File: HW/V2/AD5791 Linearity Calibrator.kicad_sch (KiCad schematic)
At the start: 47 parts, among them J11 PWR, J2 VREFP, J3 VREFN, J5 VREFP, SW1 RST, U11 L79L15, U12 7533, U13 ADuM1400xRW, U2 AD5791BRUZ, U3 ADR1399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

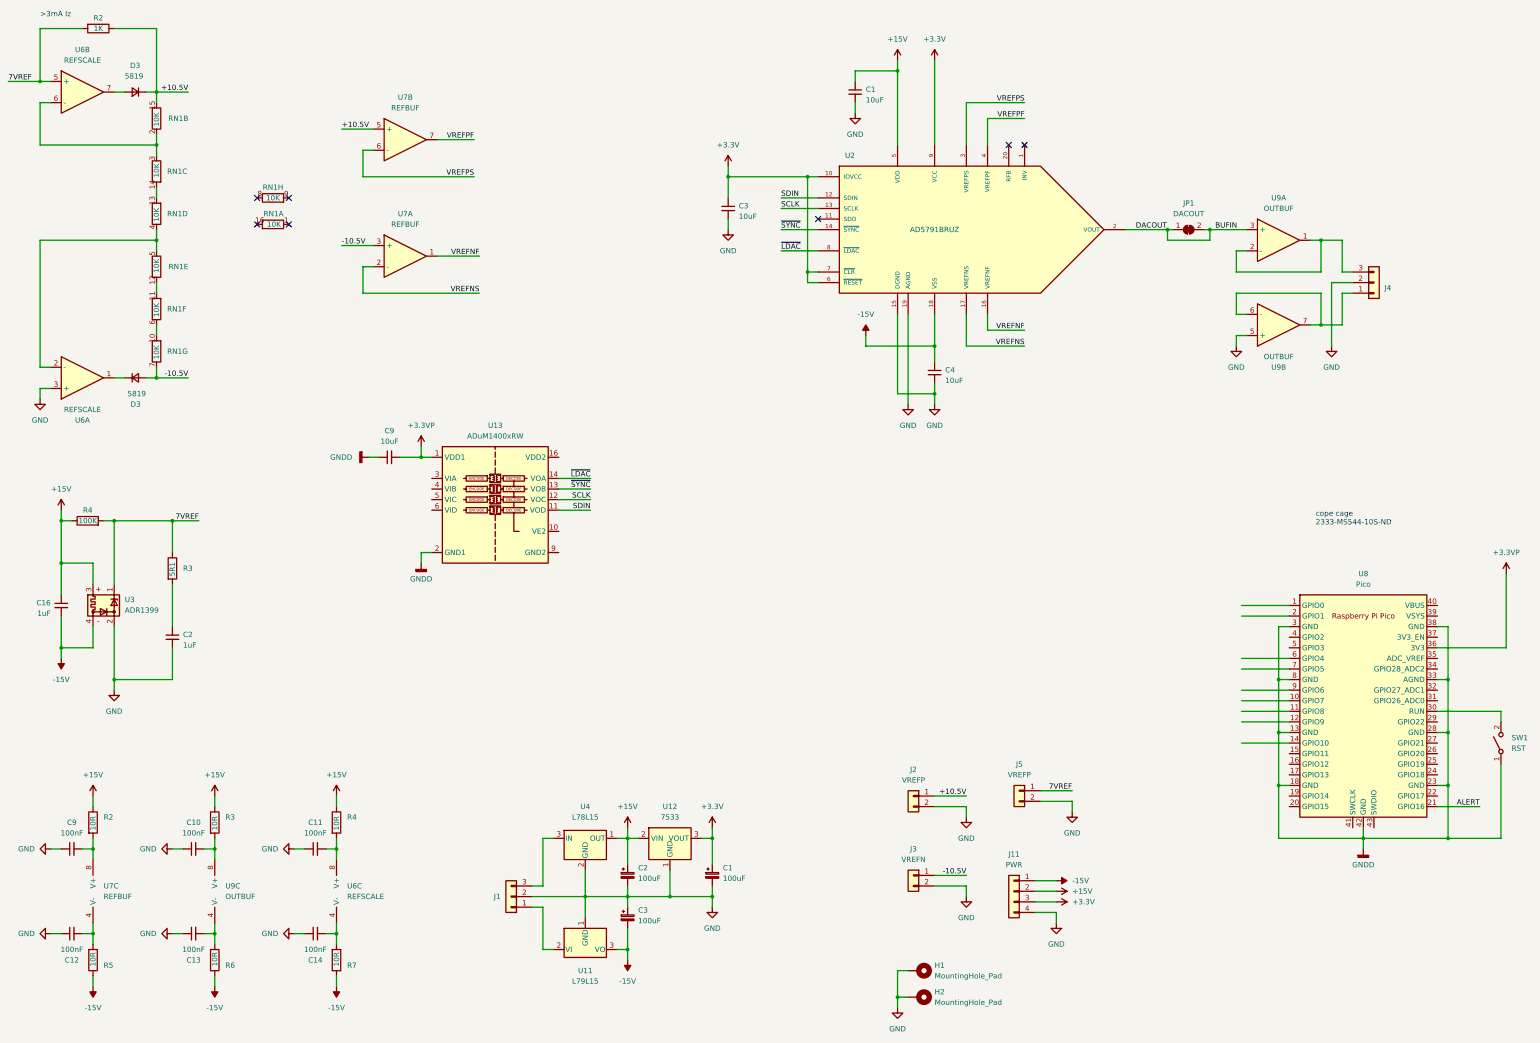
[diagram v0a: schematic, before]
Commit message: updated layout
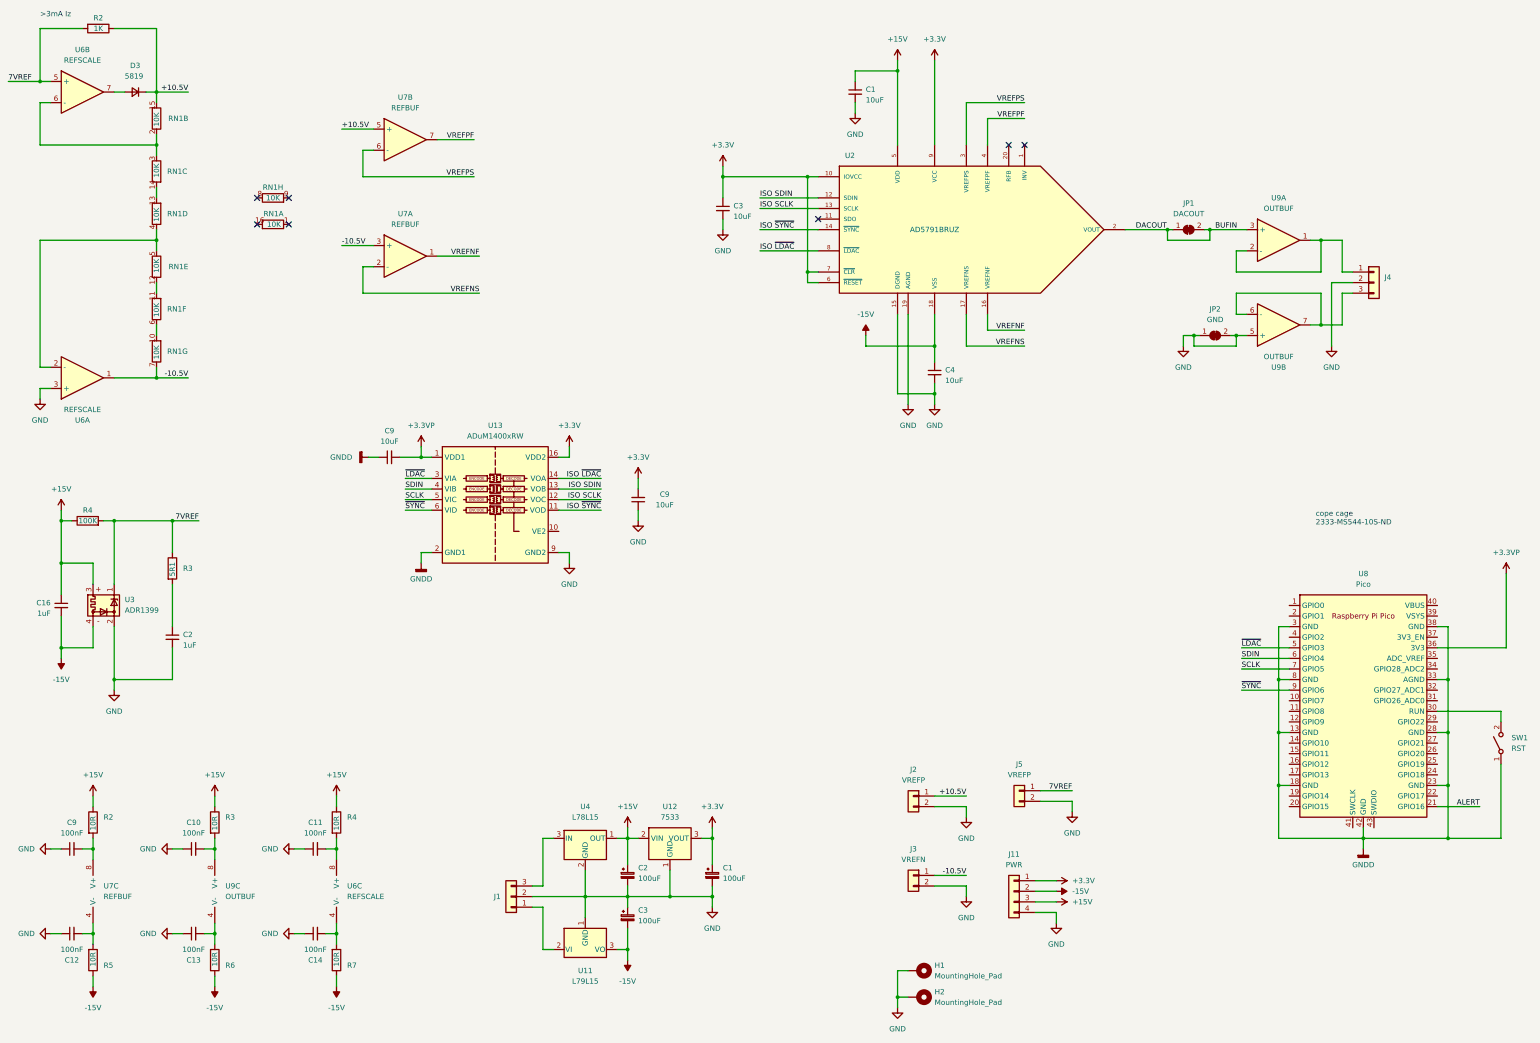
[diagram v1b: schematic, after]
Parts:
- removed D3: 5819, Resistor_SMD:R_0603_1608Metric_Pad0.98x0.95mm_HandSolder, symbol Device:D_Small
- added C9: 10uF, Resistor_SMD:R_0603_1608Metric, symbol Device:C_Small
- added JP2: GND, Connector_PinHeader_1.27mm:PinHeader_1x02_P1.27mm_Vertical, symbol Jumper:SolderJumper_2_Bridged
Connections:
- net +15V: now also J11.3 (Pin_3); no longer J11.2 (Pin_2)
- net +3.3V: now also J11.1 (Pin_1), U13.16 (VDD2), C9.2; no longer J11.3 (Pin_3)
- net -10.5V: now also U6.1
- net -15V: now also J11.2 (Pin_2); no longer J11.1 (Pin_1)
- net GND: now also U13.15 (GND2), U13.9 (GND2), C9.1, JP2.1 (A), JP2.2 (B)
- net SCLK: now also U13.5 (VIC), U8.7 (GPIO5); no longer U13.12 (VOC), U2.13 (SCLK)
- net SDIN: now also U13.4 (VIB), U8.6 (GPIO4); no longer U13.11 (VOD), U2.12 (SDIN)
- net ~{LDAC}: now also U13.3 (VIA), U8.5 (GPIO3); no longer U13.14 (VOA), U2.8 (~{LDAC})
- net ~{SYNC}: now also U13.6 (VID), U8.9 (GPIO6); no longer U13.13 (VOB), U2.14 (~{SYNC})
- net at U9.6 (-), U9.7: now also J4.3 (Pin_3); no longer J4.1 (Pin_1)
- net at U9.1, U9.2 (-): now also J4.1 (Pin_1); no longer J4.3 (Pin_3)
- new net ISO SCLK: U13.12 (VOC), U2.13 (SCLK)
- new net ISO SDIN: U13.13 (VOB), U2.12 (SDIN)
- new net ISO ~{LDAC}: U13.14 (VOA), U2.8 (~{LDAC})
- new net ISO ~{SYNC}: U13.11 (VOD), U2.14 (~{SYNC})
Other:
- moved on the sheet: C3

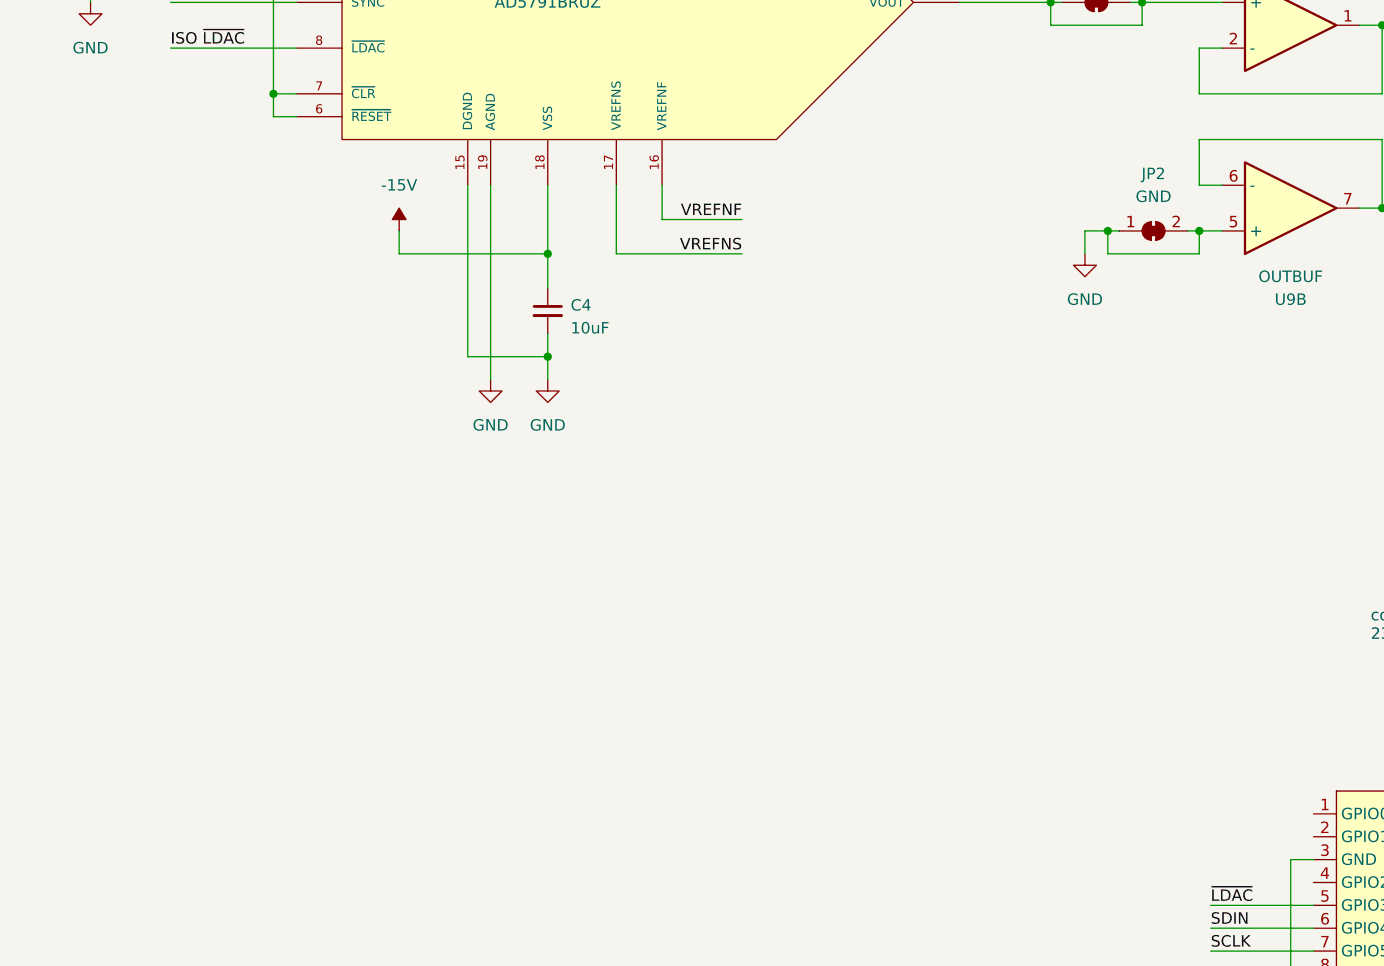
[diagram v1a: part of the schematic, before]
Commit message: updated layout
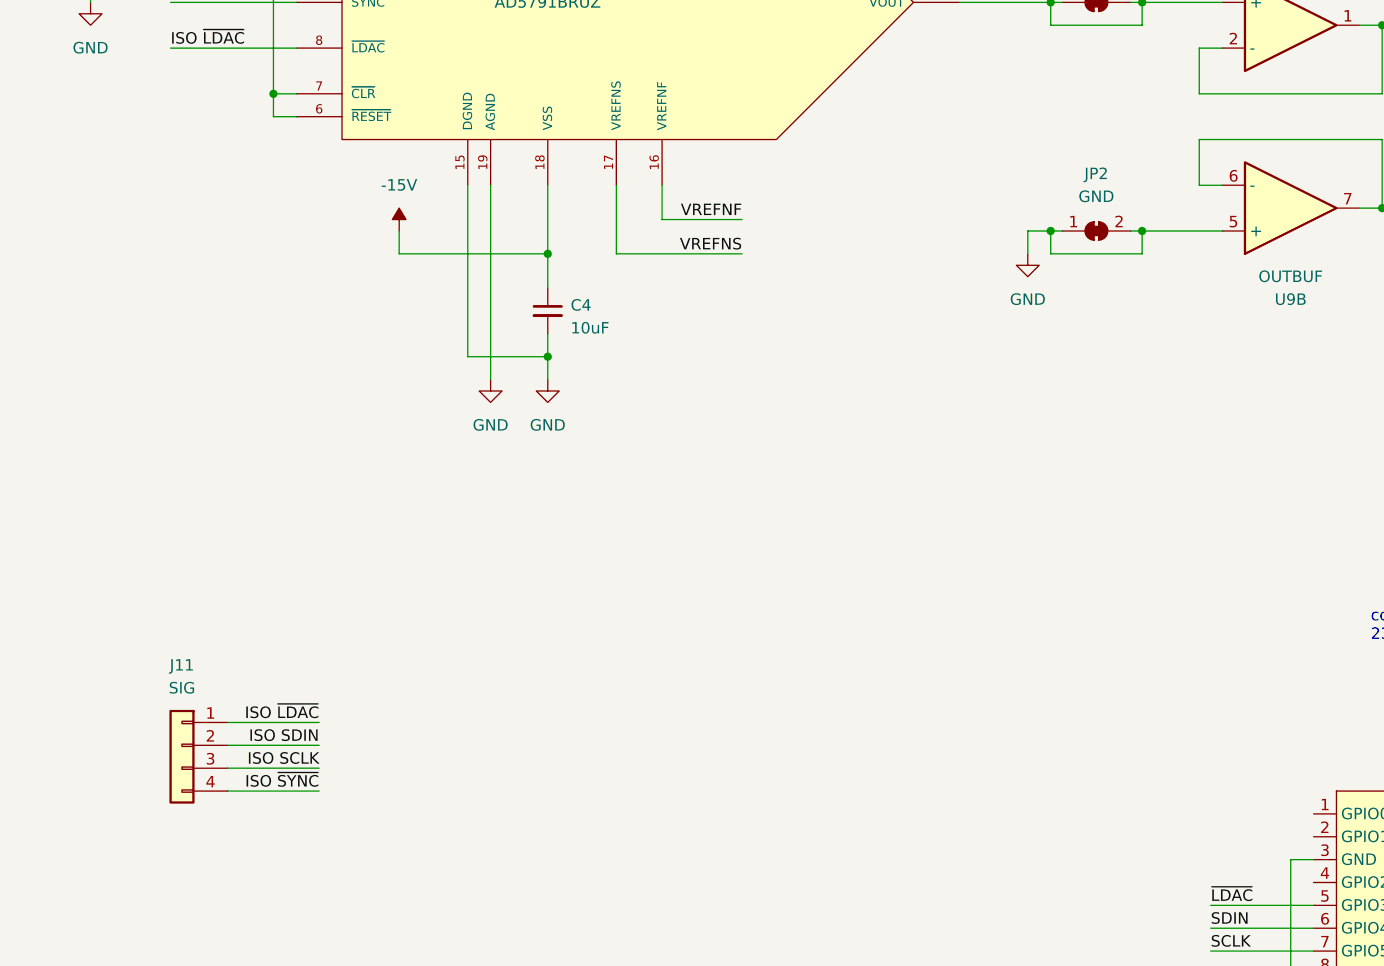
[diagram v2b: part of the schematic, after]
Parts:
- added J11: SIG, Connector_PinHeader_1.27mm:PinHeader_1x04_P1.27mm_Vertical, symbol Connector_Generic:Conn_01x04
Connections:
- net ISO SCLK: now also J11.3 (Pin_3)
- net ISO SDIN: now also J11.2 (Pin_2)
- net ISO ~{LDAC}: now also J11.1 (Pin_1)
- net ISO ~{SYNC}: now also J11.4 (Pin_4)
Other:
- moved on the sheet: JP2
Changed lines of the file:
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@@
 (kicad_sch (version 20230121) (generator eeschema)
   (paper "A3")
-  (junction (at 321.31 102.87) (diameter 0) (color 0 0 0 0)
-  )
   (junction (at 304.8 77.47) (diameter 0) (color 0 0 0 0)
   )
@@
   (junction (at 39.37 177.8) (diameter 0) (color 0 0 0 0)
   )
+  (junction (at 314.96 102.87) (diameter 0) (color 0 0 0 0)
+  )
   (junction (at 39.37 147.32) (diameter 0) (color 0 0 0 0)
   )
@@
   (junction (at 351.79 223.52) (diameter 0) (color 0 0 0 0)
   )
-  (junction (at 311.15 102.87) (diameter 0) (color 0 0 0 0)
+  (junction (at 304.8 102.87) (diameter 0) (color 0 0 0 0)
   )
   (junction (at 198.12 64.77) (diameter 0) (color 0 0 0 0)
@@
     (stroke (width 0) (type default))
   )
+  (wire (pts (xy 213.36 165.1) (xy 223.52 165.1))
+    (stroke (width 0) (type default))
+  )
   (wire (pts (xy 49.53 147.32) (xy 52.07 147.32))
     (stroke (width 0) (type default))
@@
     (stroke (width 0) (type default))
   )
+  (wire (pts (xy 213.36 157.48) (xy 223.52 157.48))
+    (stroke (width 0) (type default))
+  )
   (wire (pts (xy 158.75 144.78) (xy 168.91 144.78))
     (stroke (width 0) (type default))
@@
     (stroke (width 0) (type default))
   )
-  (wire (pts (xy 308.61 102.87) (xy 311.15 102.87))
+  (wire (pts (xy 302.26 102.87) (xy 304.8 102.87))
     (stroke (width 0) (type default))
   )
@@
     (stroke (width 0) (type default))
   )
-  (wire (pts (xy 320.04 102.87) (xy 321.31 102.87))
+  (wire (pts (xy 313.69 102.87) (xy 314.96 102.87))
     (stroke (width 0) (type default))
   )
@@
     (stroke (width 0) (type default))
   )
-  (wire (pts (xy 321.31 105.41) (xy 311.15 105.41))
+  (wire (pts (xy 314.96 105.41) (xy 304.8 105.41))
     (stroke (width 0) (type default))
   )
@@
     (stroke (width 0) (type default))
   )
-  (wire (pts (xy 321.31 102.87) (xy 323.85 102.87))
-    (stroke (width 0) (type default))
-  )
   (wire (pts (xy 341.63 80.01) (xy 346.71 80.01))
     (stroke (width 0) (type default))
@@
     (stroke (width 0) (type default))
   )
-  (wire (pts (xy 321.31 102.87) (xy 321.31 105.41))
+  (wire (pts (xy 314.96 102.87) (xy 314.96 105.41))
     (stroke (width 0) (type default))
   )
@@
     (stroke (width 0) (type default))
   )
+  (wire (pts (xy 213.36 162.56) (xy 223.52 162.56))
+    (stroke (width 0) (type default))
+  )
   (wire (pts (xy 218.44 64.77) (xy 220.98 64.77))
     (stroke (width 0) (type default))
@@
     (stroke (width 0) (type default))
   )
+  (wire (pts (xy 314.96 102.87) (xy 323.85 102.87))
+    (stroke (width 0) (type default))
+  )
   (wire (pts (xy 349.25 92.71) (xy 346.71 92.71))
     (stroke (width 0) (type default))
@@
     (stroke (width 0) (type default))
   )
+  (wire (pts (xy 213.36 160.02) (xy 223.52 160.02))
+    (stroke (width 0) (type default))
+  )
   (wire (pts (xy 331.47 185.42) (xy 331.47 198.12))
     (stroke (width 0) (type default))
@@
     (stroke (width 0) (type default))
   )
-  (wire (pts (xy 308.61 105.41) (xy 308.61 102.87))
+  (wire (pts (xy 302.26 105.41) (xy 302.26 102.87))
     (stroke (width 0) (type default))
   )
-  (wire (pts (xy 311.15 105.41) (xy 311.15 102.87))
+  (wire (pts (xy 304.8 105.41) (xy 304.8 102.87))
     (stroke (width 0) (type default))
   )
-  (wire (pts (xy 311.15 102.87) (xy 312.42 102.87))
+  (wire (pts (xy 304.8 102.87) (xy 306.07 102.87))
     (stroke (width 0) (type default))
   )
@@
     (effects (font (size 1.27 1.27)) (justify left bottom))
   )
+  (label "ISO SCLK" (at 223.52 162.56 180) (fields_autoplaced)
+    (effects (font (size 1.27 1.27)) (justify right bottom))
+  )
   (label "ISO SDIN" (at 168.91 139.7 180) (fields_autoplaced)
     (effects (font (size 1.27 1.27)) (justify right bottom))
@@
     (effects (font (size 1.27 1.27)) (justify left bottom))
   )
+  (label "ISO ~{SYNC}" (at 223.52 165.1 180) (fields_autoplaced)
+    (effects (font (size 1.27 1.27)) (justify right bottom))
+  )
   (label "+10.5V" (at 69.85 44.45 180) (fields_autoplaced)
     (effects (font (size 1.27 1.27)) (justify right bottom))
@@
     (effects (font (size 1.27 1.27)) (justify left bottom))
   )
+  (label "ISO ~{LDAC}" (at 223.52 157.48 180) (fields_autoplaced)
+    (effects (font (size 1.27 1.27)) (justify right bottom))
+  )
+  (label "ISO SDIN" (at 223.52 160.02 180) (fields_autoplaced)
+    (effects (font (size 1.27 1.27)) (justify right bottom))
+  )
   (label "7VREF" (at 281.94 212.09 180) (fields_autoplaced)
     (effects (font (size 1.27 1.27)) (justify right bottom))
@@
     )
   )
-  (symbol (lib_id "Jumper:SolderJumper_2_Bridged") (at 316.23 102.87 0) (mirror x) (unit 1)
+  (symbol (lib_id "Jumper:SolderJumper_2_Bridged") (at 309.88 102.87 0) (mirror x) (unit 1)
     (in_bom yes) (on_board yes) (dnp no) (fields_autoplaced)
-    (property "Reference" "JP2" (at 316.23 96.52 0)
+    (property "Reference" "JP2" (at 309.88 96.52 0)
       (effects (font (size 1.27 1.27)))
     )
-    (property "Value" "GND" (at 316.23 99.06 0)
+    (property "Value" "GND" (at 309.88 99.06 0)
       (effects (font (size 1.27 1.27)))
     )
-    (property "Footprint" "Connector_PinHeader_1.27mm:PinHeader_1x02_P1.27mm_Vertical" (at 316.23 102.87 0)
+    (property "Footprint" "Connector_PinHeader_1.27mm:PinHeader_1x02_P1.27mm_Vertical" (at 309.88 102.87 0)
       (effects (font (size 1.27 1.27)) hide)
     )
-    (property "Datasheet" "~" (at 316.23 102.87 0)
+    (property "Datasheet" "~" (at 309.88 102.87 0)
       (effects (font (size 1.27 1.27)) hide)
     )
@@
     )
   )
+  (symbol (lib_id "Connector_Generic:Conn_01x04") (at 208.28 160.02 0) (mirror y) (unit 1)
+    (in_bom yes) (on_board yes) (dnp no)
+    (property "Reference" "J11" (at 208.28 151.13 0)
+      (effects (font (size 1.27 1.27)))
+    )
+    (property "Value" "SIG" (at 208.28 153.67 0)
+      (effects (font (size 1.27 1.27)))
+    )
+    (property "Footprint" "Connector_PinHeader_1.27mm:PinHeader_1x04_P1.27mm_Vertical" (at 208.28 160.02 0)
+      (effects (font (size 1.27 1.27)) hide)
+    )
+    (property "Datasheet" "~" (at 208.28 160.02 0)
+      (effects (font (size 1.27 1.27)) hide)
+    )
+    (pin "1")
+    (pin "2")
+    (pin "3")
+    (pin "4")
+    (instances
+      (project "AD5791 Linearity Calibrator"
+        (path "/545249ea-2c8e-4b30-8f2b-5f4518163292"
+          (reference "J11") (unit 1)
+        )
+      )
+      (project "AD5791 Linearity Calibrator"
+        (path "/e4c8fe5c-4d6c-45a9-911b-05eafd37681e"
+          (reference "J6") (unit 1)
+        )
+      )
+    )
+  )
   (symbol (lib_id "Device:Opamp_Dual") (at 121.92 83.82 0) (unit 1)
     (in_bom yes) (on_board yes) (dnp no) (fields_autoplaced)
@@
     )
   )
-  (symbol (lib_id "power:GND") (at 308.61 105.41 0) (unit 1)
+  (symbol (lib_id "power:GND") (at 302.26 105.41 0) (unit 1)
     (in_bom yes) (on_board yes) (dnp no) (fields_autoplaced)
-    (property "Reference" "#PWR04" (at 308.61 111.76 0)
+    (property "Reference" "#PWR04" (at 302.26 111.76 0)
       (effects (font (size 1.27 1.27)) hide)
     )
-    (property "Value" "GND" (at 308.61 110.49 0)
+    (property "Value" "GND" (at 302.26 110.49 0)
       (effects (font (size 1.27 1.27)))
     )
-    (property "Footprint" "" (at 308.61 105.41 0)
+    (property "Footprint" "" (at 302.26 105.41 0)
       (effects (font (size 1.27 1.27)) hide)
     )
-    (property "Datasheet" "" (at 308.61 105.41 0)
+    (property "Datasheet" "" (at 302.26 105.41 0)
       (effects (font (size 1.27 1.27)) hide)
     )
